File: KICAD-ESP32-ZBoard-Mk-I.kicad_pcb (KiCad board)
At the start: 2 copper layers, 100 x 68.5 mm, 33 parts, among them J1 DC_Jack, J10 USB_A, J2 Conn_01x03_Pin-RAIL_1, J3 Conn_01x02_Pin-RAIL_1, J4 Conn_01x03_Pin-RAIL_2, J5 Conn_01x02_Pin-RAIL_2, J6 Conn_01x03_Pin-RAIL_3, J7 Conn_01x02_Pin-RAIL_3, J8 Conn_01x13_Pin-LEFT, J9 Conn_01x13_Pin-RIGHT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

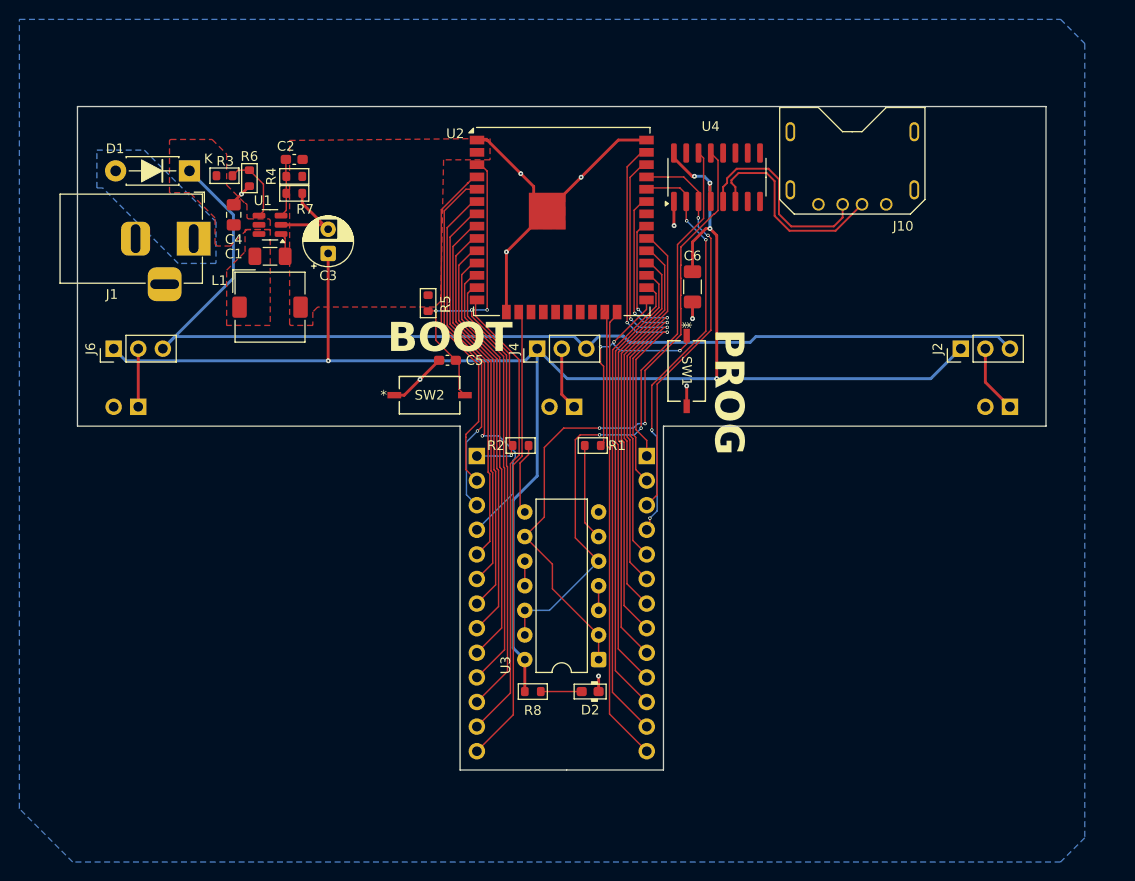
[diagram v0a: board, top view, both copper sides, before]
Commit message: ADDED silkscreen text and graphics. FIXED designator text being too small. TODO add header pin labels (very important!).
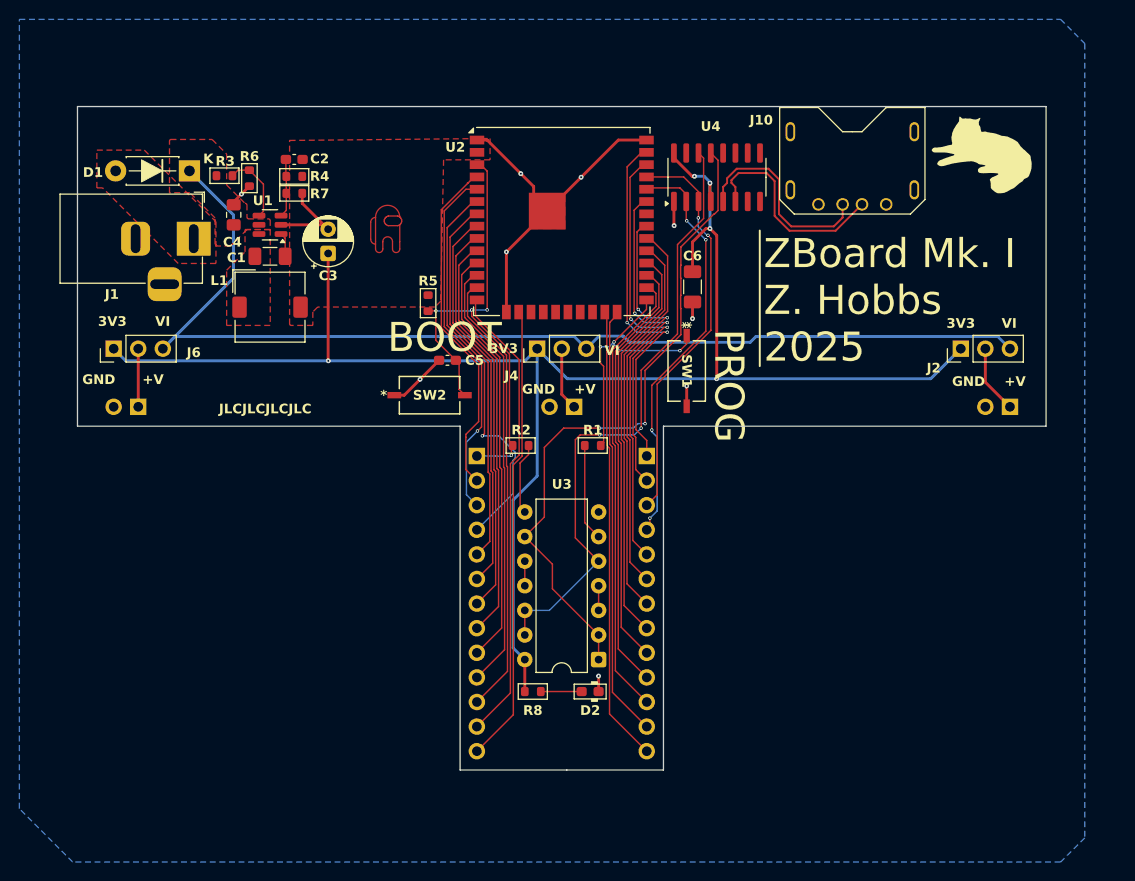
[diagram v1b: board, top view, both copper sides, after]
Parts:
- added FluffGraphic2: LOGO, ZCustomFootprints:FluffGraphic2, F.Cu at (195.6, 84.6)
- added REF**: Amogus, ZCustomFootprints:Amogus, F.Cu at (134.0, 91.6)
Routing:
- added copper zone on F.Cu, net Net-(D1-A)
- removed copper zone on B.Cu, net Net-(D1-A)
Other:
- board text added: "+V"
- board text added: "3V3"
- board text added: "GND"
- board text added: "JLCJLCJLCJLC"
- board text added: "VI"
- board text added: "ZBoard Mk. I Z. Hobbs 2025"

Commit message: ADDED all remaining pin labels. ADDED serial-breakout pins in case alternative USB is wanted.
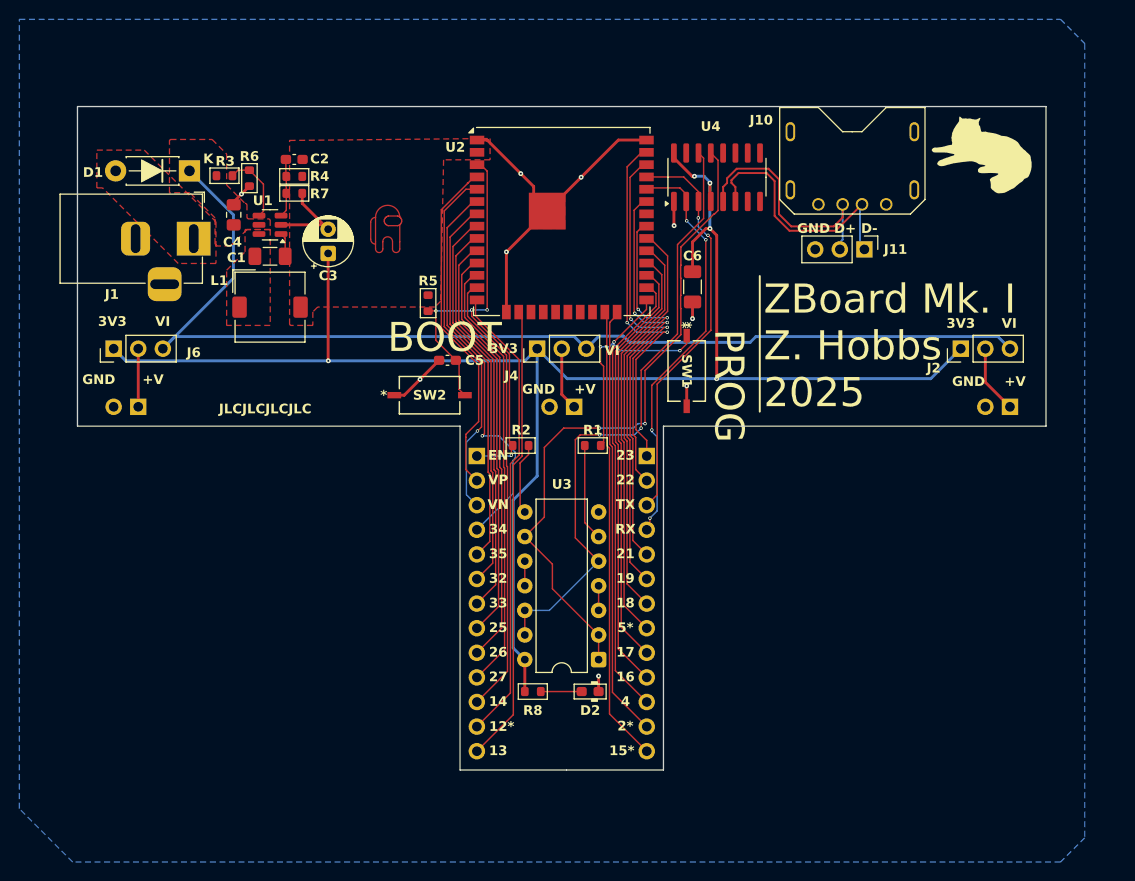
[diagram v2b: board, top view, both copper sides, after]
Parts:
- added J11: Conn_01x03-SERIAL, Connector_PinHeader_2.54mm:PinHeader_1x03_P2.54mm_Vertical, F.Cu at (183.2, 93.8)
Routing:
- net /D-: track 21.9 -> 26.8 mm
- net /D+: track 21.2 -> 26.0 mm
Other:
- board text added: "12*"
- board text added: "13"
- board text added: "14"
- board text added: "15*"
- board text added: "16"
- board text added: "17"
- board text added: "18"
- board text added: "19"
- board text added: "2*"
- board text added: "21"
- board text added: "22"
- board text added: "23"
- board text added: "25"
- board text added: "26"
- board text added: "27"
- board text added: "32"
- board text added: "33"
- board text added: "34"
- board text added: "35"
- board text added: "4"
- board text added: "5*"
- board text added: "D+"
- board text added: "D-"
- board text added: "EN"
- board text added: "RX"
- board text added: "TX"
- board text added: "VN"
- board text added: "VP"

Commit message: ADDED more cat graphics to increase PCB performance by 35%.
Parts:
- added G***: LOGO, ZCustomFootprints:FluffGraphic4, B.Cu at (114.4, 97.4)
- added G***: LOGO, ZCustomFootprints:FluffGraphic6, B.Cu at (149.0, 141.1)
- added G***: LOGO, ZCustomFootprints:FluffGraphic3, B.Cu at (128.2, 104.6)
- added G***: LOGO, ZCustomFootprints:FluffGraphic5, B.Cu at (169.9, 90.6)
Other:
- board text added: "very eepy"

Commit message: ADDED some text and finalized board.
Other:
- board text added: "eepy cat"
- board text removed: "very eepy"
